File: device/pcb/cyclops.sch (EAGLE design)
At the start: 198 parts, among them Q1 NDS351AN, Q2 NDS351AN, Q3 NDS351AN, Q4 IRF510, U1 MCP4921, U10 LT1880, U11 ZXTD, U12 DG9421, U13 THS4281, U14 ZXTD, U16 OPA1664, U2 LT1764A, U3 BD00FC0WEFJ, U4 LTM8020, U5 LT1931, U6 TPS72325, U7 TLV3701, U75 TXB0104RGYR, U8 LT1711, U9 ADR03

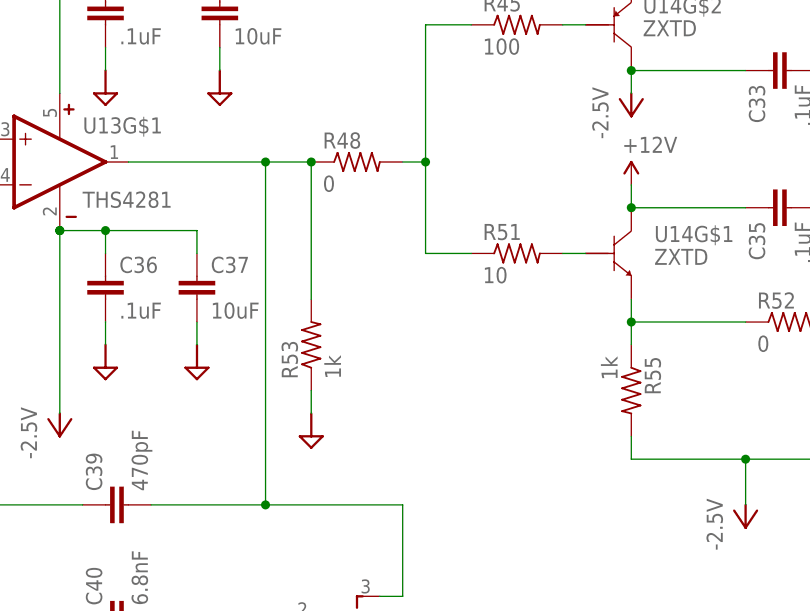
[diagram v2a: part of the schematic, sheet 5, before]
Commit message: Ready for 3.6 production
- These designs are up to date for 3.6 production
- I need to create an assembly manual before moving forward
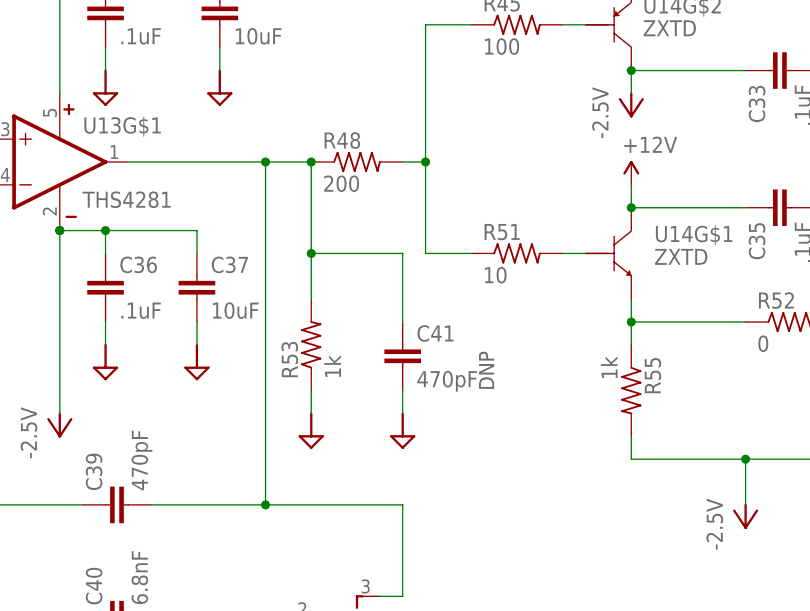
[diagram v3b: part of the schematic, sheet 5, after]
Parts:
- added C41: 470pF, cyclops:C_0603
- C12: device cyclops:C_1206 -> jonnew:C_0805
- R48: value 0 -> 200
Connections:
- net GND: now also C41.2
- net N$13: now also C41.1
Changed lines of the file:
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@@
 <part name="FRAME5" library="cyclops" deviceset="FRAME_A_L" device=""/>
 <part name="U5" library="cyclops" deviceset="LT1611" device="" value="LT1931"/>
-<part name="C12" library="cyclops" deviceset="C" device="_1206" value="1uF"/>
+<part name="C12" library="jonnew" deviceset="C" device="_0805" value="1uF"/>
 <part name="C18" library="cyclops" deviceset="C" device="_1210" value="22uF"/>
 <part name="D6" library="cyclops" deviceset="S-DIODE" device="SOD-123" value="MBR0520L"/>
@@
 <part name="VCTL&lt;&gt;CONT" library="jonnew" deviceset="SPDT" device="_AS12A*" value="AS12CV"/>
 <part name="Q1" library="jonnew" deviceset="N-MOSFET" device="_SOT23-GSD" value="NDS351AN"/>
-<part name="R48" library="cyclops" deviceset="R" device="_0603" value="0"/>
+<part name="R48" library="cyclops" deviceset="R" device="_0603" value="200"/>
 <part name="C40" library="cyclops" deviceset="C" device="_0603" value="6.8nF"/>
 <part name="C35" library="cyclops" deviceset="C" device="_0603" value=".1uF"/>
@@
 <part name="D7" library="jonnew" deviceset="S-DIODE" device="SOD-123" value="1N5819"/>
 <part name="U$13" library="cyclops" deviceset="GND2" device=""/>
+<part name="C41" library="cyclops" deviceset="C" device="_0603" value="470pF"/>
+<part name="U$12" library="cyclops" deviceset="GND2" device=""/>
 </parts>
 <sheets>
@@
 <text x="-7.62" y="124.46" size="1.6764" layer="97" rot="R90">DNP</text>
 <text x="-20.32" y="119.38" size="1.6764" layer="97" rot="R90">DNP</text>
+<text x="73.66" y="73.66" size="1.6764" layer="97" rot="R90">DNP</text>
 </plain>
 <instances>
@@
 <instance part="D7" gate="G$1" x="15.24" y="20.32" rot="R90"/>
 <instance part="U$13" gate="G$1" x="17.78" y="7.62"/>
+<instance part="C41" gate="C" x="63.5" y="78.74"/>
+<instance part="U$12" gate="G$1" x="63.5" y="68.58" rot="MR0"/>
 </instances>
 <busses>
@@
 <wire x1="17.78" y1="12.7" x2="17.78" y2="10.16" width="0.1524" layer="91"/>
 <junction x="17.78" y="12.7"/>
+</segment>
+<segment>
+<pinref part="C41" gate="C" pin="2"/>
+<wire x1="63.5" y1="73.66" x2="63.5" y2="71.12" width="0.1524" layer="91"/>
 </segment>
 </net>
@@
 <junction x="48.26" y="60.96"/>
 <pinref part="R53" gate="R" pin="2"/>
-<wire x1="53.34" y1="83.82" x2="53.34" y2="99.06" width="0.1524" layer="91"/>
+<wire x1="53.34" y1="83.82" x2="53.34" y2="88.9" width="0.1524" layer="91"/>
 <junction x="53.34" y="99.06"/>
 <pinref part="LIM&lt;BW&gt;FULL" gate="G$1" pin="3"/>
+<wire x1="53.34" y1="88.9" x2="53.34" y2="99.06" width="0.1524" layer="91"/>
 <wire x1="60.96" y1="50.8" x2="63.5" y2="50.8" width="0.1524" layer="91"/>
 <wire x1="63.5" y1="50.8" x2="63.5" y2="60.96" width="0.1524" layer="91"/>
-</segment>
-</net>
+<wire x1="53.34" y1="88.9" x2="63.5" y2="88.9" width="0.1524" layer="91"/>
+<wire x1="63.5" y1="88.9" x2="63.5" y2="81.28" width="0.1524" layer="91"/>
+<junction x="53.34" y="88.9"/>
+<pinref part="C41" gate="C" pin="1"/>
+</segment>
+</net>

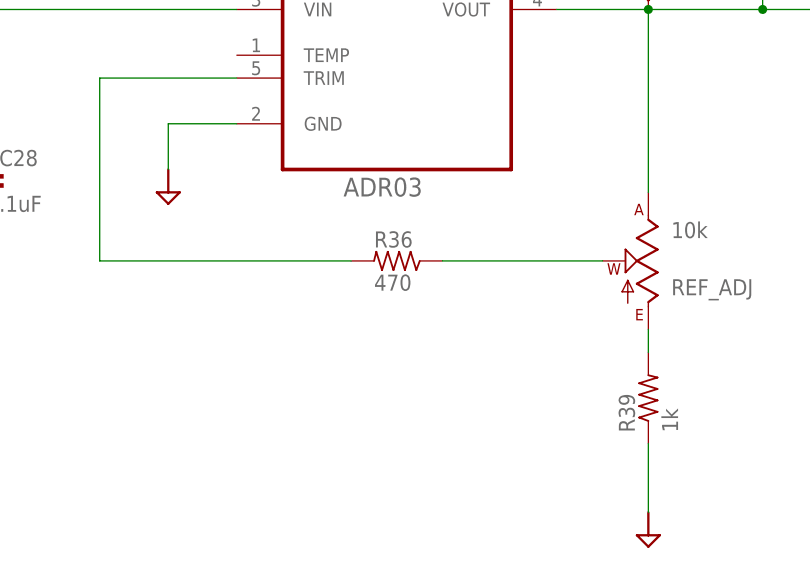
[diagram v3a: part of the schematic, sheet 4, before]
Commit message: Fixed erros found in pre-production check by Filipe.
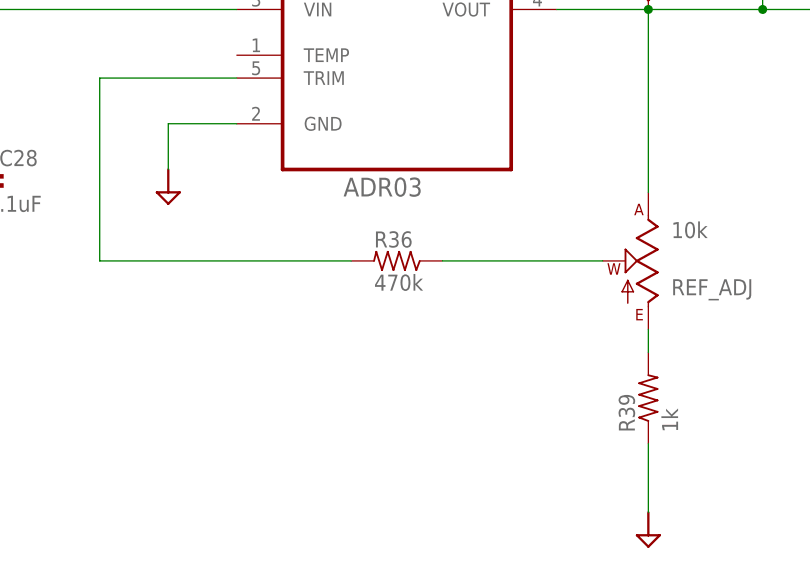
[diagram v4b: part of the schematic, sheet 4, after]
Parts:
- R36: value 470 -> 470k
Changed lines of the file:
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@@
 <?xml version="1.0" encoding="utf-8"?>
 <!DOCTYPE eagle SYSTEM "eagle.dtd">
-<eagle version="6.5.0">
+<eagle version="6.6.0">
 <drawing>
 <settings>
@@
 <part name="C27" library="cyclops" deviceset="C" device="_0805" value="1uF"/>
 <part name="C28" library="cyclops" deviceset="C" device="_0603" value=".1uF"/>
-<part name="R36" library="cyclops" deviceset="R" device="_0603" value="470"/>
+<part name="R36" library="cyclops" deviceset="R" device="_0603" value="470k"/>
 <part name="R39" library="cyclops" deviceset="R" device="_0603" value="1k"/>
 <part name="C44" library="cyclops" deviceset="C" device="_0805" value="1uF"/>

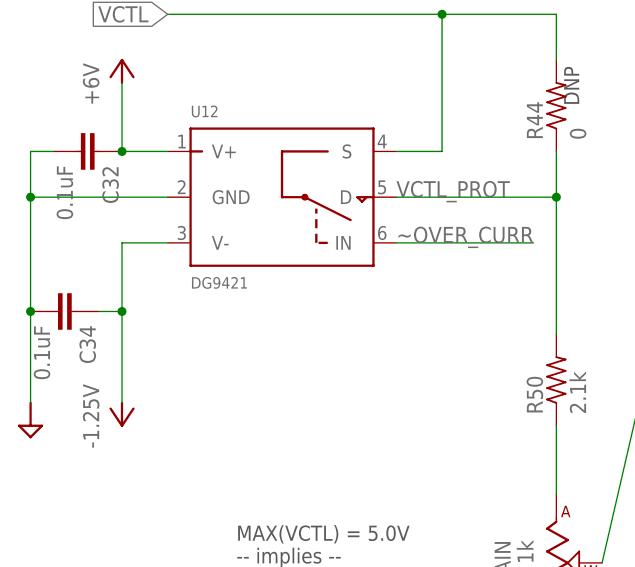
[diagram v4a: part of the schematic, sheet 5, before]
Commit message: Fixed erros found in pre-production check by Filipe.
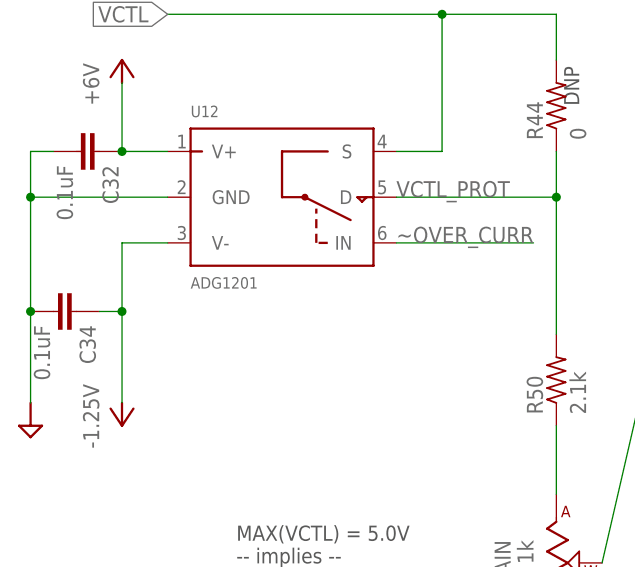
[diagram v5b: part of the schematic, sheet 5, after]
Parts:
- U12: value DG9421 -> ADG1201
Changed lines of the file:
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@@
 <part name="U$77" library="cyclops" deviceset="GND2" device=""/>
 <part name="P+1" library="jonnew" deviceset="+5V" device="" value="+6V"/>
-<part name="U12" library="jonnew" deviceset="SPST_IC" device="_SOT23-6" value="DG9421"/>
+<part name="U12" library="jonnew" deviceset="SPST_IC" device="_SOT23-6" value="ADG1201"/>
 <part name="P+9" library="jonnew" deviceset="+5V" device="" value="+6V"/>
 <part name="P+10" library="jonnew" deviceset="+5V" device="" value="+6V"/>
